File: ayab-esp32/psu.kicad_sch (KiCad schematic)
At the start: 47 parts, among them J602 Brother_DC, Q602 BCM857BV, Q603 AO3401A, U401 XL1509, U402 XL1509

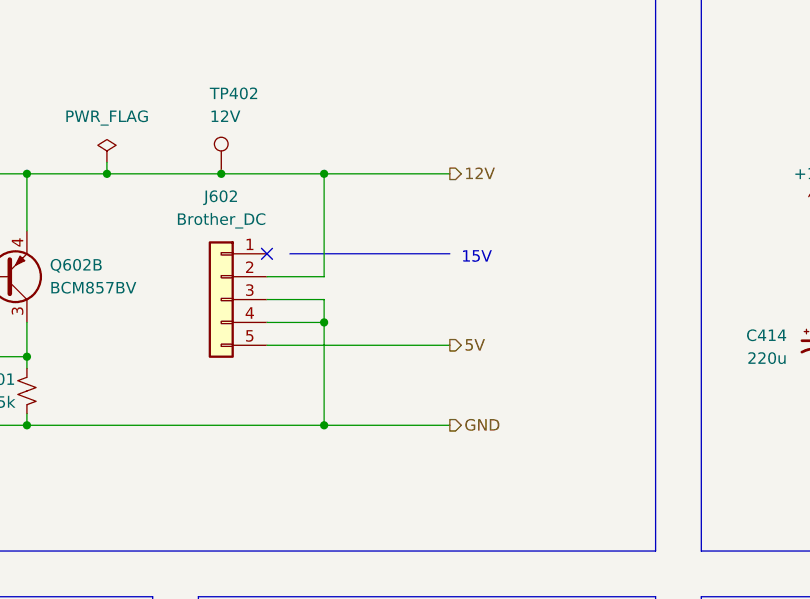
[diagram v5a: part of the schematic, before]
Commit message: comparator biasing and cleanup
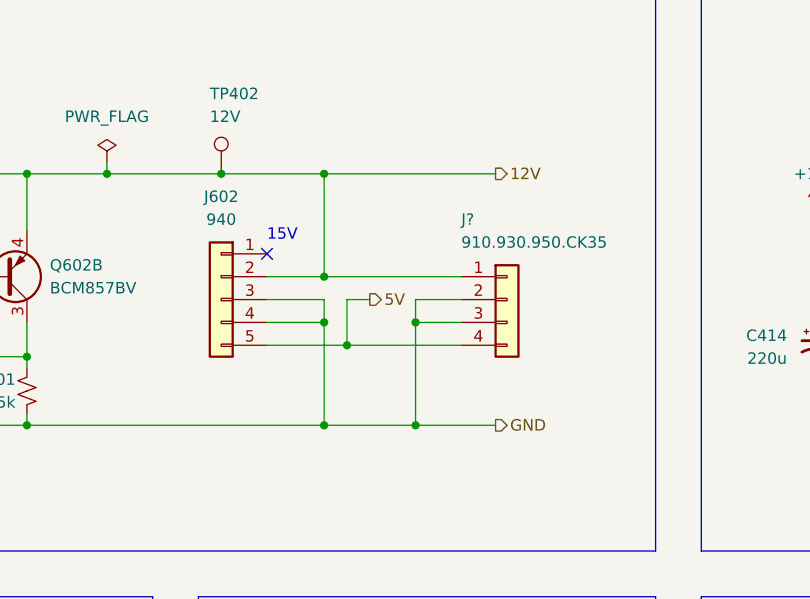
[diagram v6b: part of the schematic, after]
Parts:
- added J?: 910.930.950.CK35, symbol ayab-esp32:Conn_01x04
- J602: value Brother_DC -> 940
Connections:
- net 12V: now also J?.1 (Pin_1)
- net 5V: now also J?.4 (Pin_4)
- net GND: now also J?.2 (Pin_2), J?.3 (Pin_3)
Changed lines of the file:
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@@
   (junction (at 151.13 133.35) (diameter 0) (color 0 0 0 0)
   )
+  (junction (at 139.7 69.85) (diameter 0) (color 0 0 0 0)
+  )
   (junction (at 194.31 140.97) (diameter 0) (color 0 0 0 0)
   )
@@
   (junction (at 212.09 140.97) (diameter 0) (color 0 0 0 0)
   )
+  (junction (at 129.54 53.34) (diameter 0) (color 0 0 0 0)
+  )
   (junction (at 223.52 140.97) (diameter 0) (color 0 0 0 0)
   )
@@
   (junction (at 105.41 41.91) (diameter 0) (color 0 0 0 0)
   )
+  (junction (at 139.7 58.42) (diameter 0) (color 0 0 0 0)
+  )
   (junction (at 129.54 69.85) (diameter 0) (color 0 0 0 0)
   )
@@
   )
   (junction (at 83.82 128.27) (diameter 0) (color 0 0 0 0)
+  )
+  (junction (at 132.08 60.96) (diameter 0) (color 0 0 0 0)
   )
   (no_connect (at 123.19 50.8))
@@
     (stroke (width 0) (type default))
   )
+  (wire (pts (xy 132.08 60.96) (xy 123.19 60.96))
+    (stroke (width 0) (type default))
+  )
   (wire (pts (xy 236.22 127) (xy 236.22 132.08))
     (stroke (width 0) (type default))
@@
     (stroke (width 0) (type default))
   )
-  (polyline (pts (xy 125.73 50.8) (xy 143.51 50.8))
-    (stroke (width 0) (type default))
-  )
   (wire (pts (xy 123.19 53.34) (xy 129.54 53.34))
     (stroke (width 0) (type default))
@@
     (stroke (width 0) (type default))
   )
+  (wire (pts (xy 144.78 55.88) (xy 139.7 55.88))
+    (stroke (width 0) (type default))
+  )
   (wire (pts (xy 151.13 130.81) (xy 151.13 133.35))
     (stroke (width 0) (type default))
@@
     (stroke (width 0) (type default))
   )
+  (wire (pts (xy 132.08 55.88) (xy 132.08 60.96))
+    (stroke (width 0) (type default))
+  )
   (wire (pts (xy 83.82 118.11) (xy 93.98 118.11))
     (stroke (width 0) (type default))
@@
     (stroke (width 0) (type default))
   )
+  (wire (pts (xy 132.08 60.96) (xy 144.78 60.96))
+    (stroke (width 0) (type default))
+  )
   (polyline (pts (xy 115.57 88.9) (xy 166.37 88.9))
     (stroke (width 0) (type default))
@@
     (stroke (width 0) (type default))
   )
+  (wire (pts (xy 139.7 55.88) (xy 139.7 58.42))
+    (stroke (width 0) (type default))
+  )
   (wire (pts (xy 83.82 125.73) (xy 83.82 128.27))
     (stroke (width 0) (type default))
@@
     (stroke (width 0) (type default))
   )
-  (wire (pts (xy 129.54 69.85) (xy 143.51 69.85))
+  (wire (pts (xy 129.54 69.85) (xy 139.7 69.85))
     (stroke (width 0) (type default))
   )
@@
     (stroke (width 0) (type default))
   )
+  (wire (pts (xy 139.7 58.42) (xy 139.7 69.85))
+    (stroke (width 0) (type default))
+  )
   (wire (pts (xy 87.63 49.53) (xy 87.63 62.23))
     (stroke (width 0) (type default))
@@
     (stroke (width 0) (type default))
   )
+  (wire (pts (xy 129.54 53.34) (xy 144.78 53.34))
+    (stroke (width 0) (type default))
+  )
   (wire (pts (xy 68.58 68.58) (xy 68.58 69.85))
     (stroke (width 0) (type default))
@@
     (stroke (width 0) (type default))
   )
+  (wire (pts (xy 144.78 58.42) (xy 139.7 58.42))
+    (stroke (width 0) (type default))
+  )
   (wire (pts (xy 207.01 63.5) (xy 207.01 67.31))
     (stroke (width 0) (type default))
@@
     (stroke (width 0) (type default))
   )
-  (wire (pts (xy 129.54 41.91) (xy 143.51 41.91))
+  (wire (pts (xy 129.54 41.91) (xy 148.59 41.91))
     (stroke (width 0) (type default))
   )
@@
     (stroke (width 0) (type default))
   )
-  (wire (pts (xy 123.19 60.96) (xy 143.51 60.96))
+  (wire (pts (xy 132.08 55.88) (xy 134.62 55.88))
     (stroke (width 0) (type default))
   )
@@
   )
   (wire (pts (xy 256.54 140.97) (xy 266.7 140.97))
+    (stroke (width 0) (type default))
+  )
+  (wire (pts (xy 139.7 69.85) (xy 148.59 69.85))
     (stroke (width 0) (type default))
   )
@@
     (effects (font (size 1.27 1.27)) (justify left bottom))
   )
-  (text "15V" (at 144.78 52.07 0)
+  (text "15V" (at 123.19 49.53 0)
     (effects (font (size 1.27 1.27)) (justify left bottom))
   )
@@
     (effects (font (size 1.27 1.27)) (justify left))
   )
-  (hierarchical_label "5V" (shape output) (at 143.51 60.96 0) (fields_autoplaced)
+  (hierarchical_label "5V" (shape output) (at 134.62 55.88 0) (fields_autoplaced)
     (effects (font (size 1.27 1.27)) (justify left))
   )
@@
     (effects (font (size 1.27 1.27)) (justify left))
   )
-  (hierarchical_label "12V" (shape output) (at 143.51 41.91 0) (fields_autoplaced)
+  (hierarchical_label "12V" (shape output) (at 148.59 41.91 0) (fields_autoplaced)
     (effects (font (size 1.27 1.27)) (justify left))
   )
-  (hierarchical_label "GND" (shape output) (at 143.51 69.85 0) (fields_autoplaced)
+  (hierarchical_label "GND" (shape output) (at 148.59 69.85 0) (fields_autoplaced)
     (effects (font (size 1.27 1.27)) (justify left))
   )
@@
       (effects (font (size 1.27 1.27)))
     )
-    (property "Value" "Brother_DC" (at 118.11 46.99 0)
+    (property "Value" "940" (at 118.11 46.99 0)
       (effects (font (size 1.27 1.27)))
     )
@@
         )
       )
+    )
+  )
+  (symbol (lib_id "ayab-esp32:Conn_01x04") (at 149.86 55.88 0) (unit 1)
+    (in_bom yes) (on_board yes) (dnp no)
+    (property "Reference" "J?" (at 144.78 46.99 0)
+      (effects (font (size 1.27 1.27)) (justify left))
+    )
+    (property "Value" "910.930.950.CK35" (at 144.78 49.53 0)
+      (effects (font (size 1.27 1.27)) (justify left))
+    )
+    (property "Footprint" "" (at 149.86 55.88 0)
+      (effects (font (size 1.27 1.27)) hide)
+    )
+    (property "Datasheet" "~" (at 149.86 55.88 0)
+      (effects (font (size 1.27 1.27)) hide)
+    )
+    (pin "1")
+    (pin "2")
+    (pin "3")
+    (pin "4")
+    (instances
+      (project "ayab-esp32"
+        (path "/ad16b75f-afc8-4717-a7c6-8dd7b69a18e2/512b1de4-f8f4-4173-a7be-69b46f59a5e5"
+          (reference "J?") (unit 1)
+        )
+      )

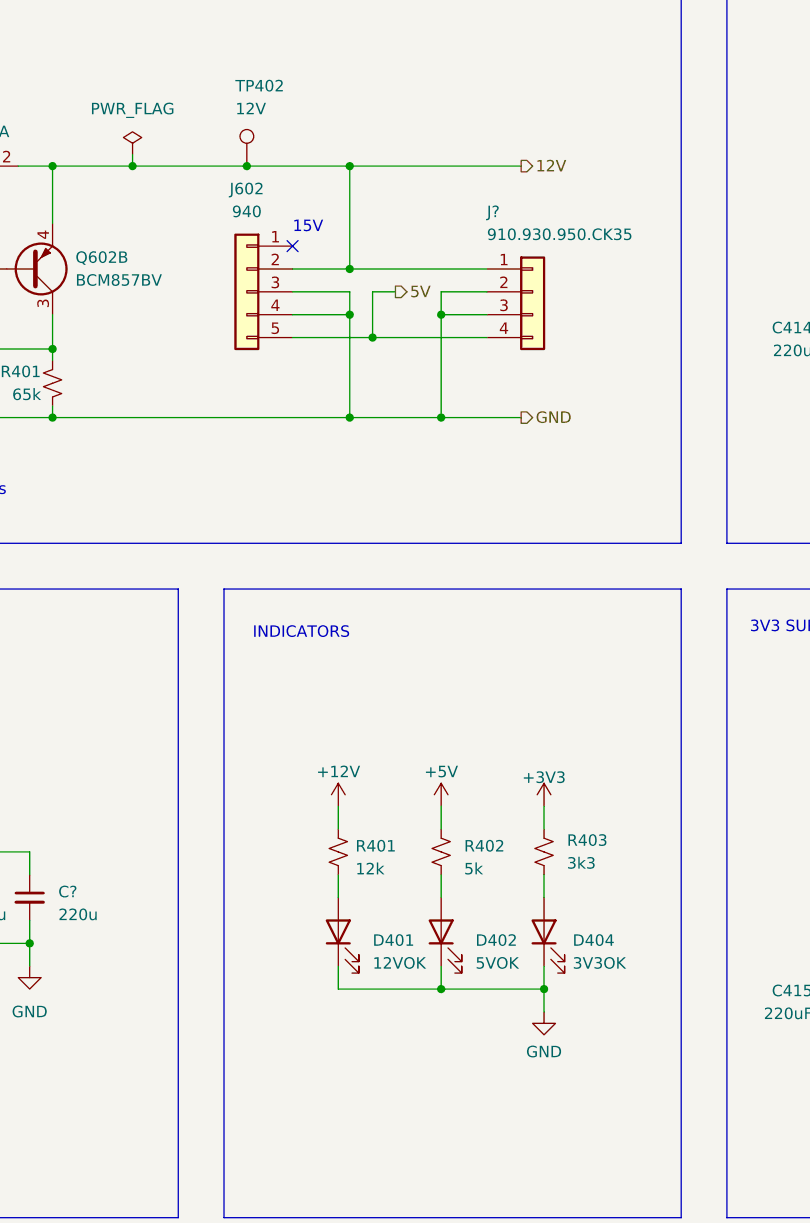
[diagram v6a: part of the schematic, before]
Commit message: fix comparator bias and hysteresis
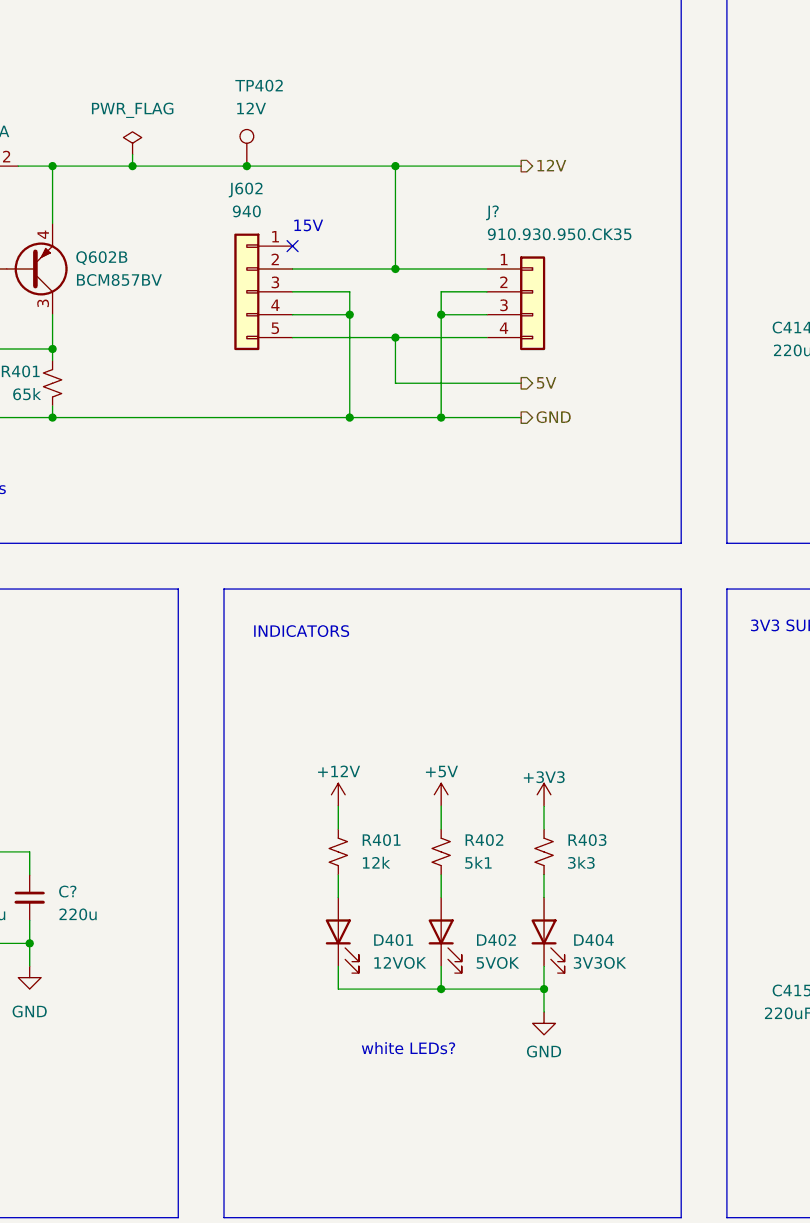
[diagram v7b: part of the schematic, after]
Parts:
- R402: value 5k -> 5k1
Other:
- note added: "white LEDs?"
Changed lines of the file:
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@@
   (junction (at 139.7 133.35) (diameter 0) (color 0 0 0 0)
   )
+  (junction (at 134.62 41.91) (diameter 0) (color 0 0 0 0)
+  )
   (junction (at 212.09 67.31) (diameter 0) (color 0 0 0 0)
   )
+  (junction (at 134.62 53.34) (diameter 0) (color 0 0 0 0)
+  )
   (junction (at 236.22 127) (diameter 0) (color 0 0 0 0)
   )
@@
   (junction (at 212.09 140.97) (diameter 0) (color 0 0 0 0)
   )
-  (junction (at 129.54 53.34) (diameter 0) (color 0 0 0 0)
-  )
   (junction (at 223.52 140.97) (diameter 0) (color 0 0 0 0)
   )
+  (junction (at 134.62 60.96) (diameter 0) (color 0 0 0 0)
+  )
   (junction (at 93.98 128.27) (diameter 0) (color 0 0 0 0)
   )
@@
   (junction (at 43.18 118.11) (diameter 0) (color 0 0 0 0)
   )
-  (junction (at 129.54 41.91) (diameter 0) (color 0 0 0 0)
-  )
   (junction (at 251.46 127) (diameter 0) (color 0 0 0 0)
   )
@@
   )
   (junction (at 83.82 128.27) (diameter 0) (color 0 0 0 0)
-  )
-  (junction (at 132.08 60.96) (diameter 0) (color 0 0 0 0)
   )
   (no_connect (at 123.19 50.8))
@@
     (stroke (width 0) (type default))
   )
+  (wire (pts (xy 123.19 60.96) (xy 134.62 60.96))
+    (stroke (width 0) (type default))
+  )
   (wire (pts (xy 123.19 58.42) (xy 129.54 58.42))
     (stroke (width 0) (type default))
@@
     (stroke (width 0) (type default))
   )
-  (wire (pts (xy 132.08 60.96) (xy 123.19 60.96))
-    (stroke (width 0) (type default))
-  )
   (wire (pts (xy 236.22 127) (xy 236.22 132.08))
     (stroke (width 0) (type default))
@@
     (stroke (width 0) (type default))
   )
+  (wire (pts (xy 134.62 53.34) (xy 144.78 53.34))
+    (stroke (width 0) (type default))
+  )
   (wire (pts (xy 234.95 39.37) (xy 232.41 39.37))
     (stroke (width 0) (type default))
   )
-  (wire (pts (xy 118.11 41.91) (xy 129.54 41.91))
-    (stroke (width 0) (type default))
-  )
   (wire (pts (xy 242.57 111.76) (xy 242.57 127))
     (stroke (width 0) (type default))
@@
     (stroke (width 0) (type default))
   )
-  (wire (pts (xy 123.19 53.34) (xy 129.54 53.34))
-    (stroke (width 0) (type default))
-  )
   (wire (pts (xy 246.38 63.5) (xy 246.38 67.31))
     (stroke (width 0) (type default))
@@
     (stroke (width 0) (type default))
   )
-  (wire (pts (xy 132.08 55.88) (xy 132.08 60.96))
+  (wire (pts (xy 134.62 66.04) (xy 134.62 60.96))
     (stroke (width 0) (type default))
   )
@@
     (stroke (width 0) (type default))
   )
+  (wire (pts (xy 134.62 41.91) (xy 148.59 41.91))
+    (stroke (width 0) (type default))
+  )
+  (wire (pts (xy 134.62 60.96) (xy 144.78 60.96))
+    (stroke (width 0) (type default))
+  )
   (wire (pts (xy 93.98 128.27) (xy 93.98 125.73))
     (stroke (width 0) (type default))
@@
     (stroke (width 0) (type default))
   )
-  (wire (pts (xy 132.08 60.96) (xy 144.78 60.96))
-    (stroke (width 0) (type default))
-  )
   (polyline (pts (xy 115.57 88.9) (xy 166.37 88.9))
     (stroke (width 0) (type default))
@@
     (stroke (width 0) (type default))
   )
-  (wire (pts (xy 129.54 53.34) (xy 129.54 41.91))
+  (wire (pts (xy 134.62 53.34) (xy 134.62 41.91))
     (stroke (width 0) (type default))
   )
@@
     (stroke (width 0) (type default))
   )
-  (wire (pts (xy 129.54 53.34) (xy 144.78 53.34))
+  (wire (pts (xy 123.19 53.34) (xy 134.62 53.34))
     (stroke (width 0) (type default))
   )
@@
     (stroke (width 0) (type default))
   )
-  (wire (pts (xy 129.54 41.91) (xy 148.59 41.91))
+  (wire (pts (xy 118.11 41.91) (xy 134.62 41.91))
     (stroke (width 0) (type default))
   )
@@
     (stroke (width 0) (type default))
   )
-  (wire (pts (xy 132.08 55.88) (xy 134.62 55.88))
+  (wire (pts (xy 134.62 66.04) (xy 148.59 66.04))
     (stroke (width 0) (type default))
   )
@@
     (effects (font (size 1.27 1.27)) (justify left bottom))
   )
+  (text "white LEDs?" (at 130.81 140.97 0)
+    (effects (font (size 1.27 1.27)) (justify left bottom))
+  )
   (text "15V" (at 123.19 49.53 0)
     (effects (font (size 1.27 1.27)) (justify left bottom))
@@
     (effects (font (size 1.27 1.27)) (justify left))
   )
-  (hierarchical_label "5V" (shape output) (at 134.62 55.88 0) (fields_autoplaced)
+  (hierarchical_label "5V" (shape output) (at 148.59 66.04 0) (fields_autoplaced)
     (effects (font (size 1.27 1.27)) (justify left))
   )
@@
   (symbol (lib_id "ayab-esp32:R_Small_US") (at 139.7 118.11 0) (unit 1)
     (in_bom yes) (on_board yes) (dnp no) (fields_autoplaced)
-    (property "Reference" "R402" (at 142.24 117.475 0)
+    (property "Reference" "R402" (at 142.24 116.84 0)
       (effects (font (size 1.27 1.27)) (justify left))
     )
-    (property "Value" "5k" (at 142.24 120.015 0)
+    (property "Value" "5k1" (at 142.24 119.38 0)
       (effects (font (size 1.27 1.27)) (justify left))
     )
@@
   )
   (symbol (lib_id "ayab-esp32:R_Small_US") (at 128.27 118.11 0) (unit 1)
-    (in_bom yes) (on_board yes) (dnp no) (fields_autoplaced)
-    (property "Reference" "R401" (at 130.175 117.475 0)
+    (in_bom yes) (on_board yes) (dnp no)
+    (property "Reference" "R401" (at 130.81 116.84 0)
       (effects (font (size 1.27 1.27)) (justify left))
     )
-    (property "Value" "12k" (at 130.175 120.015 0)
+    (property "Value" "12k" (at 130.81 119.38 0)
       (effects (font (size 1.27 1.27)) (justify left))
     )
